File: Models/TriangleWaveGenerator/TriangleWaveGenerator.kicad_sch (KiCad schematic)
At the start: 4 parts

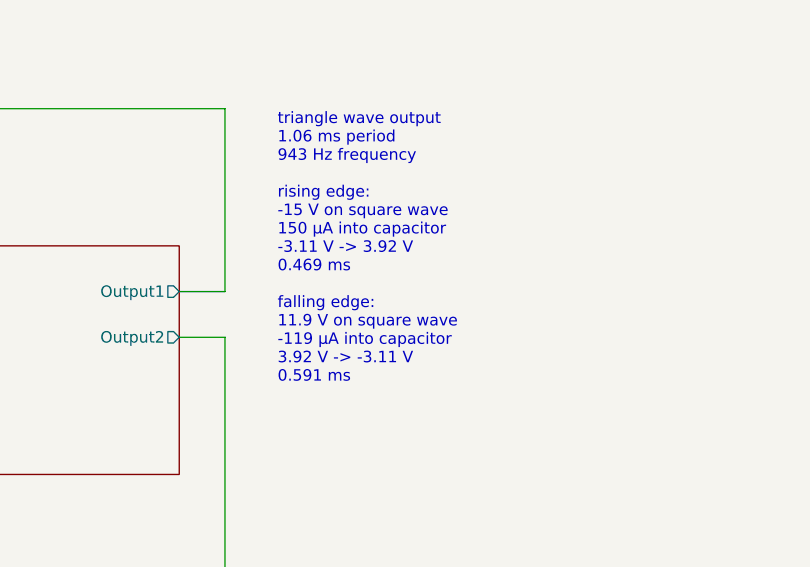
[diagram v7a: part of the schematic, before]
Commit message: Corrected the sign of the currents
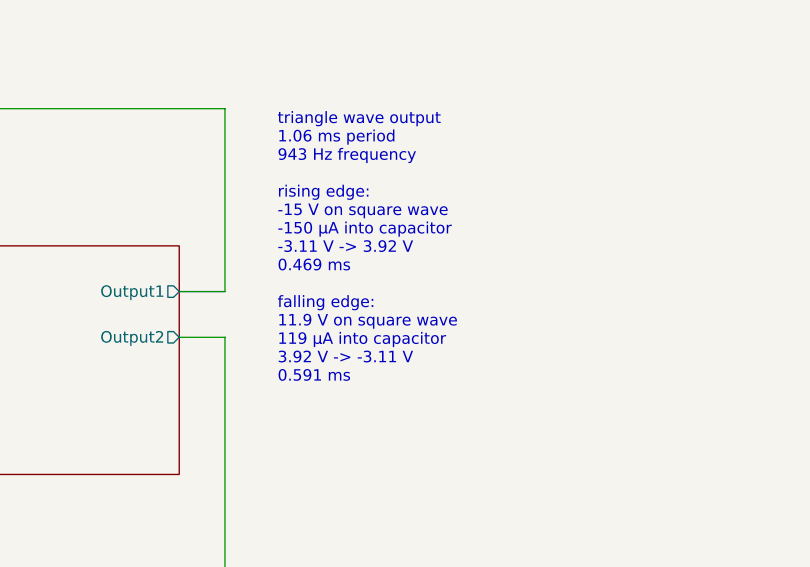
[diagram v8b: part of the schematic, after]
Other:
- note added: "triangle wave output 1.06 ms period 943 Hz frequency rising edge: -15 V on square wave -150 μA into capacitor -3.11 V -> 3.92 V 0.469 ms falling edge: 11.9 V on square wave 119 μA into capacitor 3.92 V -> -3.11 V 0.591 ms"
- note removed: "triangle wave output 1.06 ms period 943 Hz frequency rising edge: -15 V on square wave 150 μA into capacitor -3.11 V -> 3.92 V 0.469 ms falling edge: 11.9 V on square wave -119 μA into capacitor 3.92 V -> -3.11 V 0.591 ms"
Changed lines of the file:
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@@
 		)
 	)
-	(text "triangle wave output\n1.06 ms period\n943 Hz frequency\n\nrising edge:\n-15 V on square wave\n150 μA into capacitor\n-3.11 V -> 3.92 V\n0.469 ms\n\nfalling edge:\n11.9 V on square wave\n-119 μA into capacitor\n3.92 V -> -3.11 V\n0.591 ms"
+	(text "triangle wave output\n1.06 ms period\n943 Hz frequency\n\nrising edge:\n-15 V on square wave\n-150 μA into capacitor\n-3.11 V -> 3.92 V\n0.469 ms\n\nfalling edge:\n11.9 V on square wave\n119 μA into capacitor\n3.92 V -> -3.11 V\n0.591 ms"
 		(exclude_from_sim no)
 		(at 137.922 48.768 0)
